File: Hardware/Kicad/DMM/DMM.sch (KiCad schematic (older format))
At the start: 4 parts

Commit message: Continued development on USB-C to FIFO Bridge
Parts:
- removed P?: USB_C_Plug-Connector, symbol DBLS_USB:USB_C_Plug-Connector
- removed U? (x2): ADS7251, symbol DBLS_Data_Converters:ADS7251
- added C? (x2): SMD-CAP-1UF-0402, DBLS_Capacitor:C_0402_1005Metric, symbol DBLS_Capacitor:SMD-CAP-1UF-0402
- added C?: SMD-CAP-4.7UF-0402, DBLS_Capacitor:C_0402_1005Metric, symbol DBLS_Capacitor:SMD-CAP-4.7UF-0402
- added C? (x2): SMD-CAP-100NF-0402, DBLS_Capacitor:C_0402_1005Metric, symbol DBLS_Capacitor:SMD-CAP-100NF-0402
- added J?: USB_C_Receptacle, symbol DBLS_USB:USB_C_Receptacle
- added R?: SMD-RES-10K-0603, DBLS_Resistor:R_0603_1608Metric_Pad1.05x0.95mm_HandSolder, symbol DBLS_Resistor:SMD-RES-10K-0603
- added R?: SMD-RES-0-0603, Resistors_SMD:R_0603, symbol DBLS_Resistor:SMD-RES-0-0603
- added R?: SMD-RES-0-0603, DBLS_Resistor:R_0603_1608Metric_Pad1.05x0.95mm_HandSolder, symbol DBLS_Resistor:SMD-RES-0-0603
- added U? (x2): TPD4E05U06, symbol DBLS_Diode:TPD4E05U06
- added U? (x4): ESD122, symbol DBLS_Diode:ESD122
- added U?: LP5912, DBLS_SON:WSON-6-1EP_2x2mm_P0.65mm_EP1x1.6mm_ThermalVias, symbol DBLS_LDO:LP5912
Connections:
- net labels added: CC1, CC2, D+, D-, FIFO_DATA_BUS, GND, LDO_EN, LDO_PG, RX+, RX-, SBU1, SBU2, TX+, TX-, VBUS
- wire segments 0 -> 119
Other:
- note added: "Ferrite may\nbe needed"
- moved on the sheet: U?

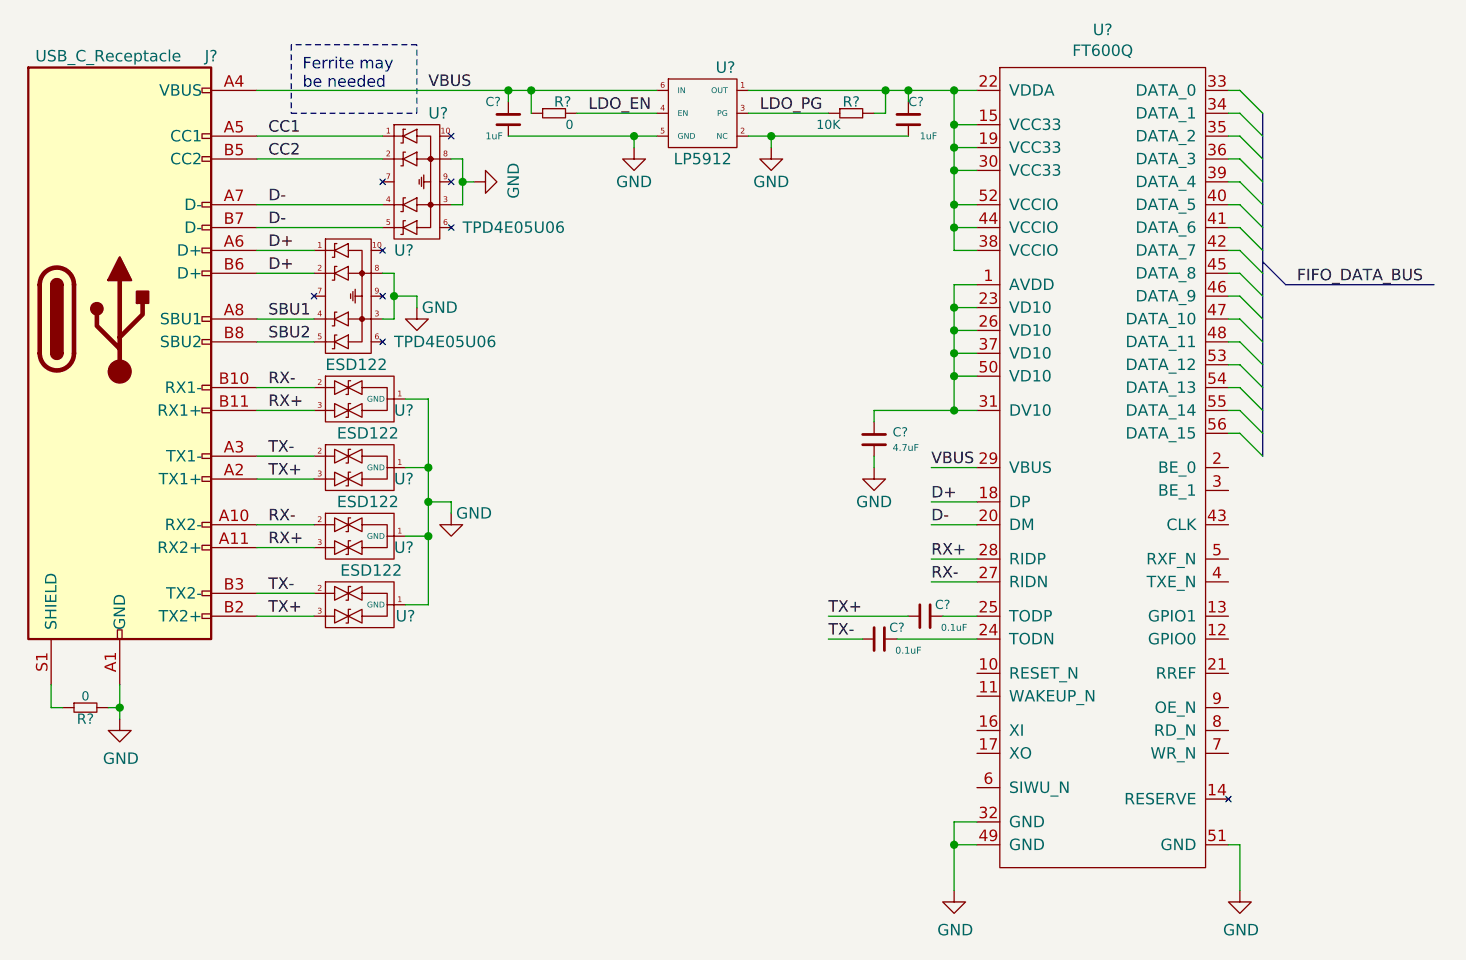
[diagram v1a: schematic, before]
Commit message: Continued schematic development on USB to FIFO bridge and began AFE schematic development
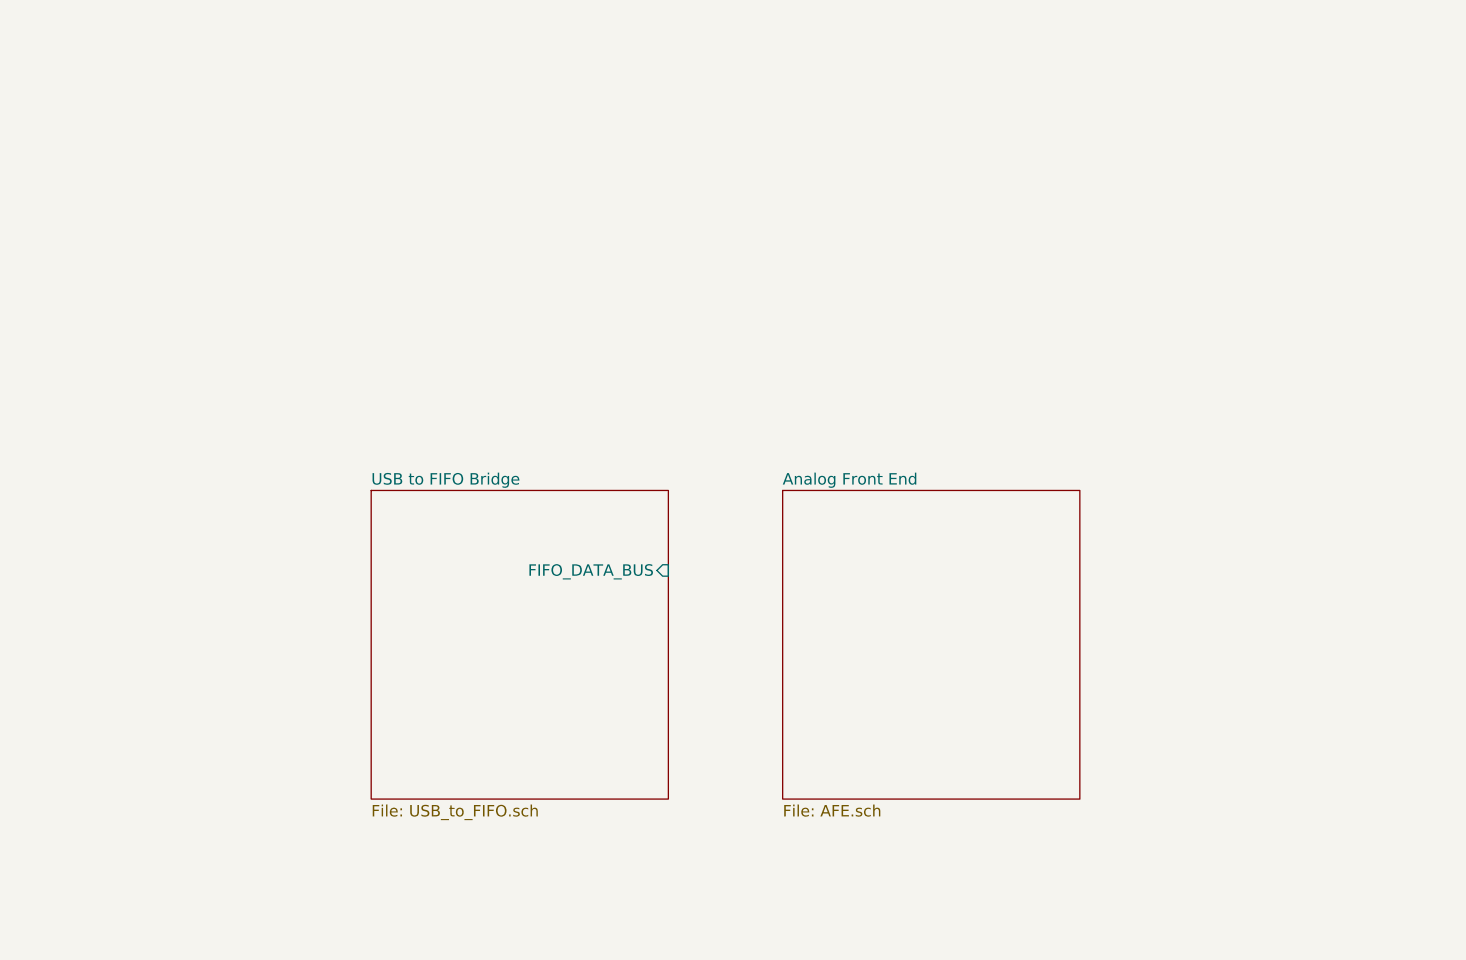
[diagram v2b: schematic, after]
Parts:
- removed C? (x2): SMD-CAP-1UF-0402, DBLS_Capacitor:C_0402_1005Metric, symbol DBLS_Capacitor:SMD-CAP-1UF-0402
- removed C?: SMD-CAP-4.7UF-0402, DBLS_Capacitor:C_0402_1005Metric, symbol DBLS_Capacitor:SMD-CAP-4.7UF-0402
- removed C? (x2): SMD-CAP-100NF-0402, DBLS_Capacitor:C_0402_1005Metric, symbol DBLS_Capacitor:SMD-CAP-100NF-0402
- removed J?: USB_C_Receptacle, symbol DBLS_USB:USB_C_Receptacle
- removed R?: SMD-RES-10K-0603, DBLS_Resistor:R_0603_1608Metric_Pad1.05x0.95mm_HandSolder, symbol DBLS_Resistor:SMD-RES-10K-0603
- removed R?: SMD-RES-0-0603, Resistors_SMD:R_0603, symbol DBLS_Resistor:SMD-RES-0-0603
- removed R?: SMD-RES-0-0603, DBLS_Resistor:R_0603_1608Metric_Pad1.05x0.95mm_HandSolder, symbol DBLS_Resistor:SMD-RES-0-0603
- removed U?: FT600Q, symbol DBLS_USB:FT600Q
- removed U? (x2): TPD4E05U06, symbol DBLS_Diode:TPD4E05U06
- removed U? (x4): ESD122, symbol DBLS_Diode:ESD122
- removed U?: LP5912, DBLS_SON:WSON-6-1EP_2x2mm_P0.65mm_EP1x1.6mm_ThermalVias, symbol DBLS_LDO:LP5912
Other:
- note removed: "Ferrite may\nbe needed"

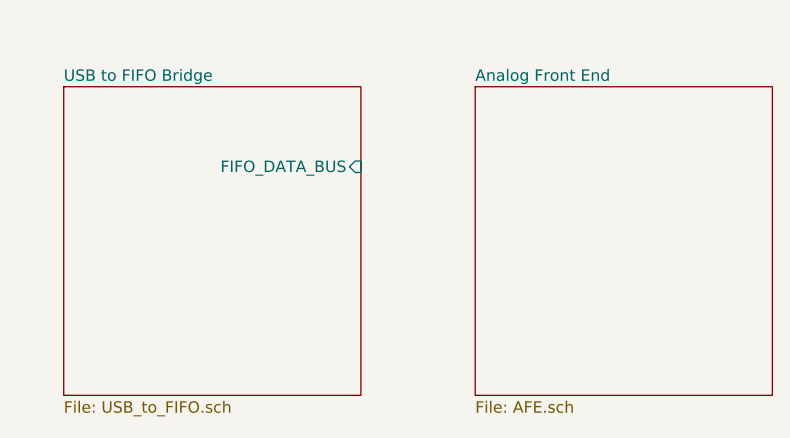
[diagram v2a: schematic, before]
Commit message: Continued AFE schematic developement, adding anti-alias filter, reference buffer, and gain stages.
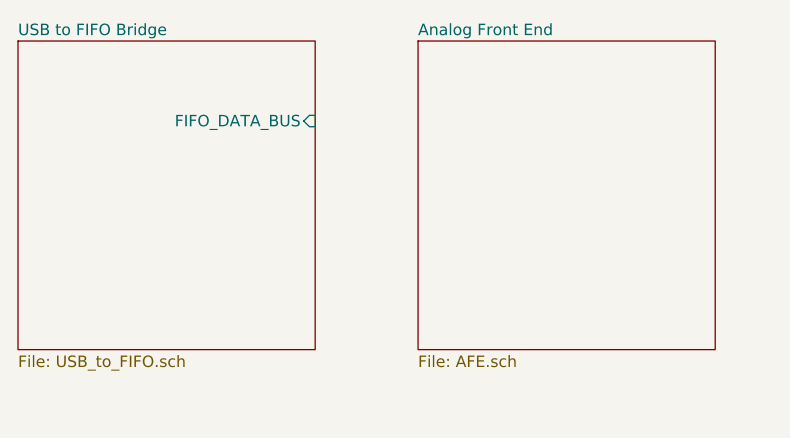
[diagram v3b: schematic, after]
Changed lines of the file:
@@
 $EndDescr
 $Sheet
-S 2200 2650 1300 1350
+S 2000 2450 1300 1350
 U 5E81C490
 F0 "USB to FIFO Bridge" 50
 F1 "USB_to_FIFO.sch" 50
-F2 "FIFO_DATA_BUS" I R 3500 3000 50
+F2 "FIFO_DATA_BUS" I R 3300 2800 50
 $EndSheet
 $Sheet
-S 4000 2650 1300 1350
+S 3750 2450 1300 1350
 U 5E8627B4
 F0 "Analog Front End" 50
